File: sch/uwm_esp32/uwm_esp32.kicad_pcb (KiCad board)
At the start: 2 copper layers, 2 parts, among them U1 DWM3000TR13, U2 XIAO_ESP32C3

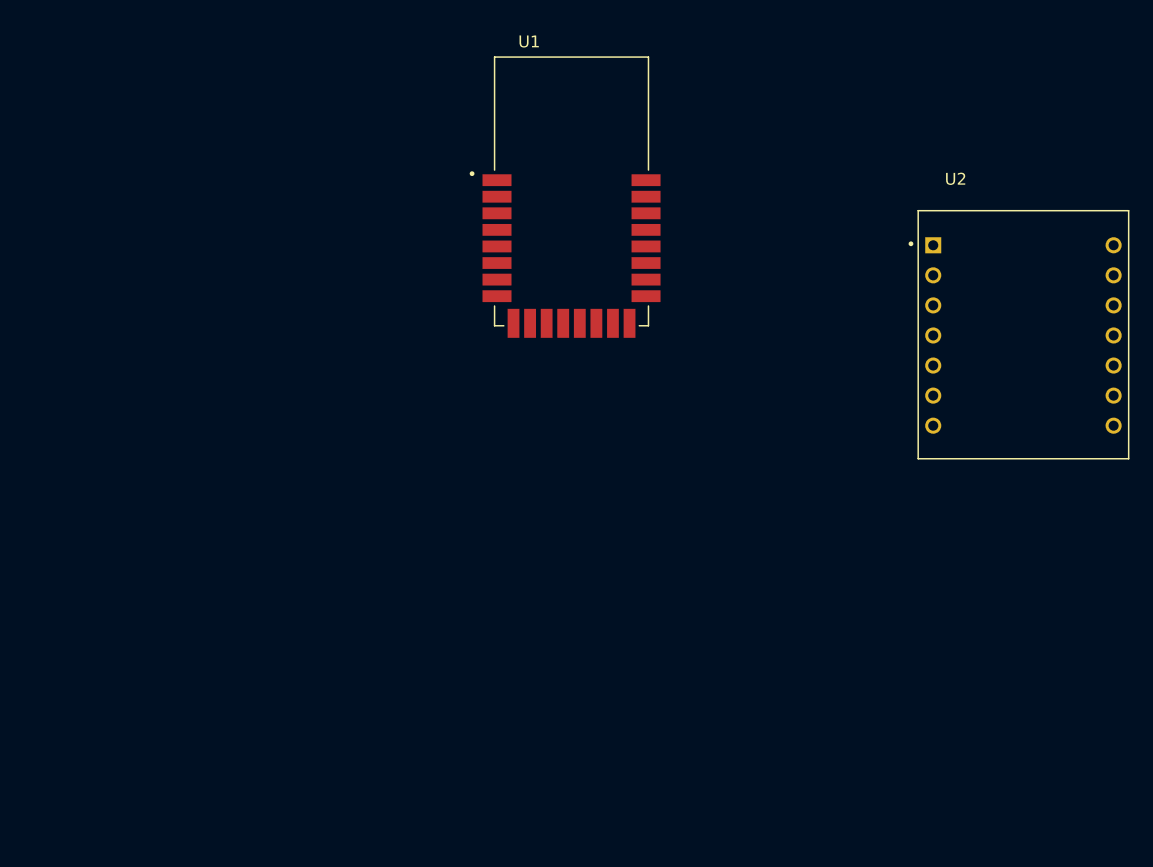
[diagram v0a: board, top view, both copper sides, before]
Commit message: Add ESP32 and DWM edge headers
Replace test points with six-pin edge headers, connect the ESP32-C3 and DWM3000 signals, and update the PCB layout with the module and supporting components.
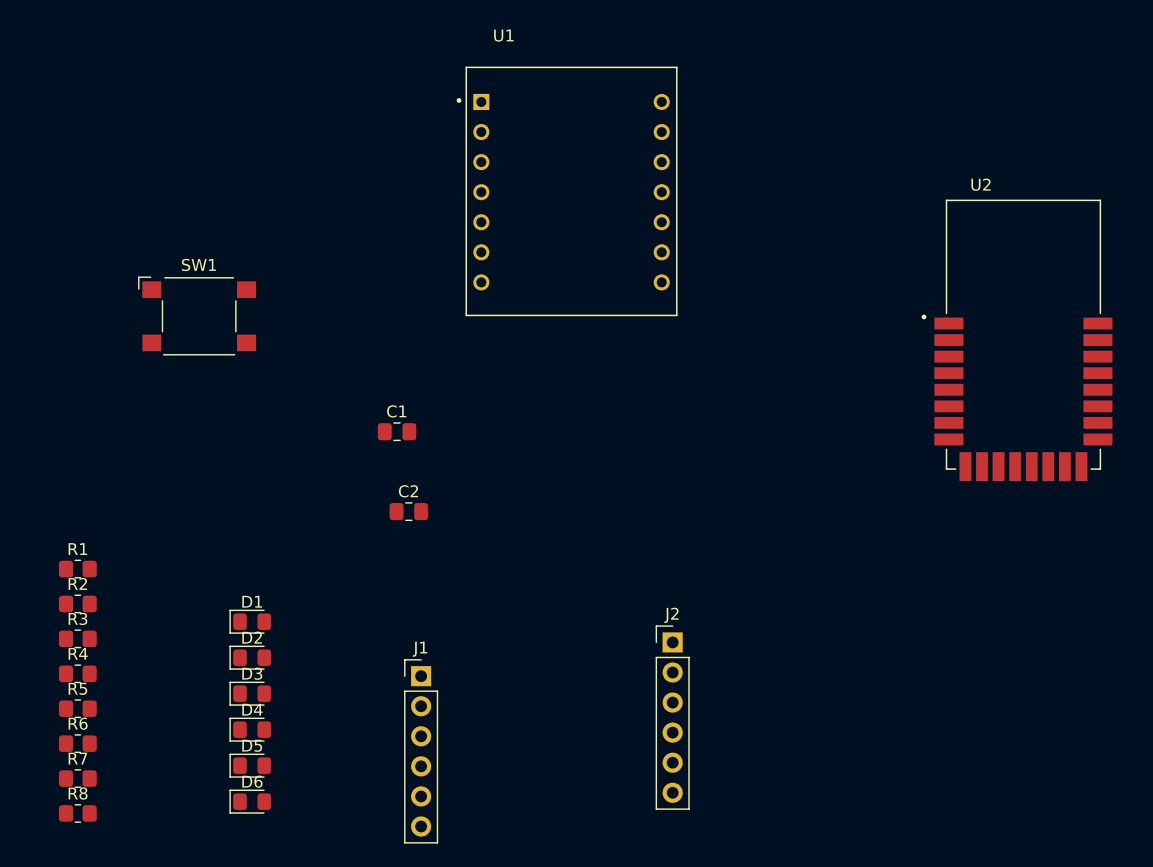
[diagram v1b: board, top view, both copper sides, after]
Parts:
- added C1: 100n, Capacitor_SMD:C_0805_2012Metric_Pad1.18x1.45mm_HandSolder, F.Cu at (103.0, 69.2)
- added C2: 10u, Capacitor_SMD:C_0805_2012Metric_Pad1.18x1.45mm_HandSolder, F.Cu at (104.0, 76.0)
- added D1: Tag, LED_SMD:LED_0805_2012Metric_Pad1.15x1.40mm_HandSolder, F.Cu at (90.7, 85.3)
- added D2: Anchor, LED_SMD:LED_0805_2012Metric_Pad1.15x1.40mm_HandSolder, F.Cu at (90.7, 88.3)
- added D3: LED, LED_SMD:LED_0805_2012Metric_Pad1.15x1.40mm_HandSolder, F.Cu at (90.7, 91.4)
- added D4: LED, LED_SMD:LED_0805_2012Metric_Pad1.15x1.40mm_HandSolder, F.Cu at (90.7, 94.4)
- added D5: LED, LED_SMD:LED_0805_2012Metric_Pad1.15x1.40mm_HandSolder, F.Cu at (90.7, 97.5)
- added D6: LED, LED_SMD:LED_0805_2012Metric_Pad1.15x1.40mm_HandSolder, F.Cu at (90.7, 100.5)
- added J1: ESP32 Edge Header, Connector_PinHeader_2.54mm:PinHeader_1x06_P2.54mm_Vertical, F.Cu at (105.0, 89.9)
- added J2: DWM Edge Header, Connector_PinHeader_2.54mm:PinHeader_1x06_P2.54mm_Vertical, F.Cu at (126.2, 87.0)
- added R1: 1k, Resistor_SMD:R_0805_2012Metric_Pad1.20x1.40mm_HandSolder, F.Cu at (76.0, 80.8)
- added R2: 1k, Resistor_SMD:R_0805_2012Metric_Pad1.20x1.40mm_HandSolder, F.Cu at (76.0, 83.8)
- added R3: 1k, Resistor_SMD:R_0805_2012Metric_Pad1.20x1.40mm_HandSolder, F.Cu at (76.0, 86.8)
- added R4: 1k, Resistor_SMD:R_0805_2012Metric_Pad1.20x1.40mm_HandSolder, F.Cu at (76.0, 89.7)
- added R5: 1k, Resistor_SMD:R_0805_2012Metric_Pad1.20x1.40mm_HandSolder, F.Cu at (76.0, 92.7)
- added R6: 1k, Resistor_SMD:R_0805_2012Metric_Pad1.20x1.40mm_HandSolder, F.Cu at (76.0, 95.6)
- added R7: 100k, Resistor_SMD:R_0805_2012Metric_Pad1.20x1.40mm_HandSolder, F.Cu at (76.0, 98.5)
- added R8: 10k, Resistor_SMD:R_0805_2012Metric_Pad1.20x1.40mm_HandSolder, F.Cu at (76.0, 101.5)
- added SW1: Sleep Button, Button_Switch_SMD:SW_SPST_Omron_B3FS-101xP, F.Cu at (86.2, 59.5)
- U1: value DWM3000TR13 -> XIAO_ESP32C3; footprint uwb_esp32:XCVR_DWM3000TR13 -> uwb_esp32:MODULE_XIAO_ESP32C3
- U2: value XIAO_ESP32C3 -> DWM3000TR13; footprint uwb_esp32:MODULE_XIAO_ESP32C3 -> uwb_esp32:XCVR_DWM3000TR13
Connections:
- U1 pad 1: unconnected-(U1-EXTON-Pad1) -> /D0
- U1 pad 10: unconnected-(U1-GPIO5/EXTTXE/SPIPOL-Pad10) -> /D9
- U1 pad 11: unconnected-(U1-GPIO4-Pad11) -> /IRQ
- U1 pad 12: unconnected-(U1-GPIO3/TXLED-Pad12) -> +3V3
- U1 pad 13: unconnected-(U1-GPIO2/RXLED-Pad13) -> GND
- U1 pad 14: unconnected-(U1-GPIO1/SFDLED-Pad14) -> +5V
- U1 pad 2: unconnected-(U1-WAKEUP-Pad2) -> Net-(U1-D1)
- U1 pad 3: unconnected-(U1-~{RST}-Pad3) -> /SPIMISO
- U1 pad 4: unconnected-(U1-GPIO7/SYNC-Pad4) -> /SPICSn
- U1 pad 5: +3V3 -> /SPICLK
- U1 pad 6: +3V3 -> /SPIMOSI
- U1 pad 7: +3V3 -> /ModeLED
- U1 pad 8: GND -> /RSTn
- U1 pad 9: unconnected-(U1-GPIO6/EXTRXE/SPIPHA-Pad9) -> /D8
- U2 pad 1: unconnected-(U2-D0-Pad1) -> /EXTON
- U2 pad 10: unconnected-(U2-D9-Pad10) -> /SPIPOL
- U2 pad 11: unconnected-(U2-D10-Pad11) -> /GPIO4
- U2 pad 12: +3V3 -> /TXLED
- U2 pad 13: GND -> /RXLED
- U2 pad 14: unconnected-(U2-VUSB-Pad14) -> /SFDLED
- U2 pad 2: unconnected-(U2-D1-Pad2) -> GND
- U2 pad 3: unconnected-(U2-D2-Pad3) -> /RSTn
- U2 pad 4: unconnected-(U2-D3-Pad4) -> /SYNC
- U2 pad 5: unconnected-(U2-D4-Pad5) -> +3V3
- U2 pad 6: unconnected-(U2-D5-Pad6) -> +3V3
- U2 pad 7: unconnected-(U2-TX_D6-Pad7) -> +3V3
- U2 pad 8: unconnected-(U2-RX_D7-Pad8) -> GND
- U2 pad 9: unconnected-(U2-D8-Pad9) -> /SPIPHA

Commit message: Revise ESP32 UWB board layout
Reposition and lock components, add M3 mounting holes, antenna keepout, and silkscreen labels. Update PCB design settings.
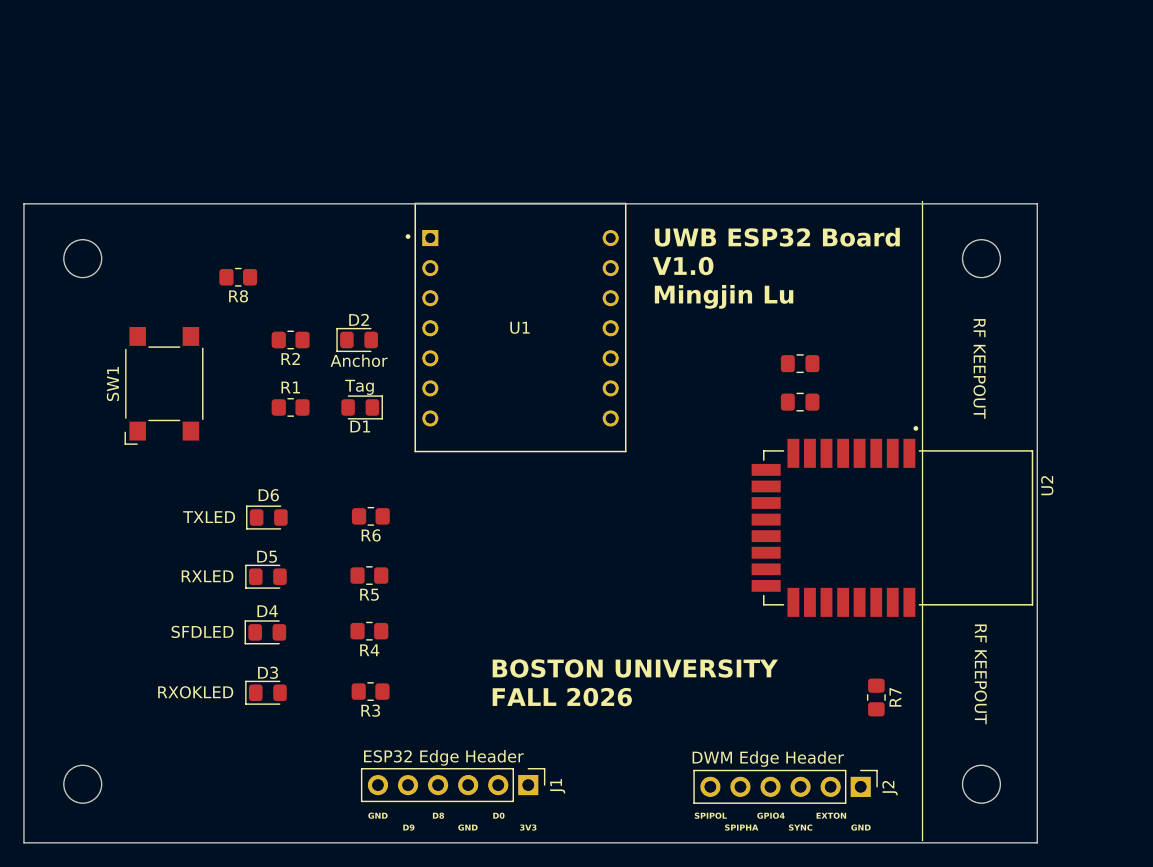
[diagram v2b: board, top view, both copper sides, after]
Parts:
- added REF**: MountingHole_3.2mm_M3, MountingHole:MountingHole_3.2mm_M3, F.Cu at (76.4, 99.0)
- added REF**: MountingHole_3.2mm_M3, MountingHole:MountingHole_3.2mm_M3, F.Cu at (76.4, 54.6)
- added REF**: MountingHole_3.2mm_M3, MountingHole:MountingHole_3.2mm_M3, F.Cu at (152.3, 54.6)
- added REF**: MountingHole_3.2mm_M3, MountingHole:MountingHole_3.2mm_M3, F.Cu at (152.3, 99.0)
- D3: value LED -> RXOKLED
- D4: value LED -> SFDLED
- D5: value LED -> RXLED
- D6: value LED -> TXLED
- moved R7 67.8 mm to (143.5, 91.7), turned to -90 degrees
- moved R8 47.3 mm to (89.6, 56.2), turned to 180 degrees
- moved C2 35.3 mm to (137.0, 63.5), turned to 180 degrees
- moved C1 34.1 mm to (137.0, 66.8), turned to 180 degrees
- moved R6 31.3 mm to (100.8, 76.4), turned to 180 degrees
- moved R2 28.6 mm to (94.0, 61.5), turned to 180 degrees
- moved D2 28.3 mm to (99.8, 61.5)
- moved R5 27.1 mm to (100.6, 81.4), turned to 180 degrees
- moved R3 25.1 mm to (100.7, 91.2), turned to 180 degrees
- moved R4 24.9 mm to (100.6, 86.1), turned to 180 degrees
- moved D6 24.0 mm to (92.1, 76.5)
- moved R1 22.6 mm to (94.0, 67.2)
- moved D1 20.3 mm to (99.9, 67.2), turned to 180 degrees
- moved J2 20.0 mm to (142.1, 99.2), turned to -90 degrees
- moved U2 19.4 mm to (145.3, 77.4), turned to -90 degrees
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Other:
- board outline added: 85.6 x 54 mm
- board text added: "3V3"
- board text added: "BOSTON UNIVERSITY FALL 2026"
- board text added: "D0"
- board text added: "D8"
- board text added: "D9"
- board text added: "EXTON"
- board text added: "GND"
- board text added: "GPIO4"
- board text added: "RF KEEPOUT"
- board text added: "SPIPHA"
- board text added: "SPIPOL"
- board text added: "SYNC"
- board text added: "UWB ESP32 Board V1.0 Mingjin Lu"

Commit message: Adjust ESP32 PCB component placement
Reposition and rotate C1/C2, increase the through-hole pad drill to 1 mm, and update the PCB pad-size defaults.
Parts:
- moved C2 5.16 mm to (140.2, 67.6), turned to 90 degrees
- moved C1 1.27 mm to (138.0, 67.6), turned to 90 degrees
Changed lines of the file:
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@@
 		(capping no)
 		(filling no)
-		(zone_defaults)
 		(grid_origin 157.055 104)
 		(pcbplotparams
@@
 			(at 7.62 -7.5565)
 			(size 1.358 1.358)
-			(drill 0.85)
+			(drill 1)
 			(layers "*.Cu" "*.Mask")
 			(remove_unused_layers no)
@@
 	)
 	(footprint "Capacitor_SMD:C_0805_2012Metric_Pad1.18x1.45mm_HandSolder"
-		(locked yes)
 		(layer "F.Cu")
-		(at 137.0175 66.75 180)
+		(at 137.955 67.6 90)
 		(descr "Capacitor SMD 0805 (2012 Metric), square (rectangular) end terminal, IPC-7351 nominal with elongated pad for handsoldering. (Body size source: IPC-SM-782 page 76, https://www.pcb-3d.com/wordpress/wp-content/uploads/ipc-sm-782a_amendment_1_and_2.pdf, https://docs.google.com/spreadsheets/d/1BsfQQcO9C6DZCsRaXUlFlo91Tg2WpOkGARC1WS5S8t0/edit?usp=sharing)")
 		(tags "capacitor handsolder")
 		(property "Reference" "C1"
-			(at 0 -1.68 0)
+			(at 0 -1.68 90)
 			(layer "F.SilkS")
 			(hide yes)
@@
 		)
 		(property "Value" "100n"
-			(at 3.7875 -0.25 0)
+			(at 3.7875 -0.25 90)
 			(layer "F.Fab")
 			(effects
@@
 		)
 		(property "Datasheet" ""
-			(at 0 0 0)
+			(at 0 0 90)
 			(layer "F.Fab")
 			(hide yes)
@@
 		)
 		(property "Description" "Unpolarized capacitor, small symbol"
-			(at 0 0 0)
+			(at 0 0 90)
 			(layer "F.Fab")
 			(hide yes)
@@
 		)
 		(property "KiLib_Generator" "SMD_2terminal_chip_molded"
-			(at 0 0 0)
+			(at 0 0 90)
 			(layer "F.SilkS")
 			(hide yes)
@@
 		(duplicate_pad_numbers_are_jumpers no)
 		(fp_line
-			(start -0.261252 0.735)
-			(end 0.261252 0.735)
+			(start -0.261252 -0.735)
+			(end 0.261252 -0.735)
 			(stroke
 				(width 0.12)
@@
 		)
 		(fp_line
-			(start -0.261252 -0.735)
-			(end 0.261252 -0.735)
+			(start -0.261252 0.735)
+			(end 0.261252 0.735)
 			(stroke
 				(width 0.12)
@@
 		)
 		(fp_text user "${REFERENCE}"
-			(at 0 0 0)
+			(at 0 0 90)
 			(layer "F.Fab")
 			(effects
@@
 		)
 		(pad "1" smd roundrect
-			(at -1.0375 0 180)
+			(at -1.0375 0 90)
 			(size 1.175 1.45)
 			(layers "F.Cu" "F.Mask" "F.Paste")
@@
 		)
 		(pad "2" smd roundrect
-			(at 1.0375 0 180)
+			(at 1.0375 0 90)
 			(size 1.175 1.45)
 			(layers "F.Cu" "F.Mask" "F.Paste")
@@
 	)
 	(footprint "Capacitor_SMD:C_0805_2012Metric_Pad1.18x1.45mm_HandSolder"
-		(locked yes)
 		(layer "F.Cu")
-		(at 137.0175 63.5 180)
+		(at 140.155 67.6 90)
 		(descr "Capacitor SMD 0805 (2012 Metric), square (rectangular) end terminal, IPC-7351 nominal with elongated pad for handsoldering. (Body size source: IPC-SM-782 page 76, https://www.pcb-3d.com/wordpress/wp-content/uploads/ipc-sm-782a_amendment_1_and_2.pdf, https://docs.google.com/spreadsheets/d/1BsfQQcO9C6DZCsRaXUlFlo91Tg2WpOkGARC1WS5S8t0/edit?usp=sharing)")
 		(tags "capacitor handsolder")
 		(property "Reference" "C2"
-			(at 0 -1.68 0)
+			(at 0 -1.68 90)
 			(layer "F.SilkS")
 			(hide yes)
@@
 		)
 		(property "Value" "10u"
-			(at 3.7875 0 0)
+			(at 3.7875 0 90)
 			(layer "F.Fab")
 			(effects
@@
 		)
 		(property "Datasheet" ""
-			(at 0 0 0)
+			(at 0 0 90)
 			(layer "F.Fab")
 			(hide yes)
@@
 		)
 		(property "Description" "Unpolarized capacitor, small symbol"
-			(at 0 0 0)
+			(at 0 0 90)
 			(layer "F.Fab")
 			(hide yes)
@@
 		)
 		(property "KiLib_Generator" "SMD_2terminal_chip_molded"
-			(at 0 0 0)
+			(at 0 0 90)
 			(layer "F.SilkS")
 			(hide yes)
@@
 		(duplicate_pad_numbers_are_jumpers no)
 		(fp_line
-			(start -0.261252 0.735)
-			(end 0.261252 0.735)
+			(start -0.261252 -0.735)
+			(end 0.261252 -0.735)
 			(stroke
 				(width 0.12)
@@
 		)
 		(fp_line
-			(start -0.261252 -0.735)
-			(end 0.261252 -0.735)
+			(start -0.261252 0.735)
+			(end 0.261252 0.735)
 			(stroke
 				(width 0.12)
@@
 		)
 		(fp_text user "${REFERENCE}"
-			(at 0 0 0)
+			(at 0 0 90)
 			(layer "F.Fab")
 			(effects
@@
 		)
 		(pad "1" smd roundrect
-			(at -1.0375 0 180)
+			(at -1.0375 0 90)
 			(size 1.175 1.45)
 			(layers "F.Cu" "F.Mask" "F.Paste")
@@
 		)
 		(pad "2" smd roundrect
-			(at 1.0375 0 180)
+			(at 1.0375 0 90)
 			(size 1.175 1.45)
 			(layers "F.Cu" "F.Mask" "F.Paste")
